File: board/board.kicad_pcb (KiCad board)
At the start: 2 copper layers, 66 x 48.3 mm, 93 parts, among them IC1 SN74LVC245APWR, IC2 SN74LVC245APWR, IC3 SN74LVC245APWR, IC4 SN74LVC245APWR, IC5 AP3417C, IC6 AP3417C, P1 CONN_02X16, P2 POWER, P3 JTAG, P4 HDMI-A, P5 CONN_01X03, SW1 SKRWAEE030, U1 10M08SCE144C8G, U2 ADV7513, U3 LFSPXO025560

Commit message: Schematics and Start of Board Layout
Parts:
- removed C10, C8: 4.7u, Capacitors_SMD:C_0805_HandSoldering
- removed C26, C27, C28, C29, C30, C35, C36, C37, C38, C39, C40, C41, C42, C43, C44, C45: 100nF, Capacitors_SMD:C_0805_HandSoldering
- removed C9: 10uF, Capacitors_SMD:C_0805_HandSoldering
- removed D1, D2: LED, LEDs:LED_0805
- removed F1: 0ZCK0050AF2E, Capacitors_SMD:C_0805_HandSoldering
- removed IC1, IC2, IC3, IC4: SN74LVC245APWR, Housings_SSOP:TSSOP-20_4.4x6.5mm_Pitch0.65mm
- removed IC5, IC6: AP3417C, TO_SOT_Packages_SMD:TSOT-23-5_HandSoldering
- removed L3, L4, L5, L6, L7: 10uH, Capacitors_SMD:C_0805_HandSoldering
- removed L8, L9: 2.2uH, Capacitors_SMD:C_0805_HandSoldering
- removed P1: CONN_02X16, Pin_Headers:Pin_Header_Straight_2x16_Pitch2.54mm
- removed P2: POWER, Pin_Headers:Pin_Header_Straight_1x02_Pitch2.54mm
- removed P3: JTAG, Pin_Headers:Pin_Header_Straight_2x05_Pitch2.54mm
- removed P4: HDMI-A, footprints:FCI_10029449-11-5B13-5DRLF
- removed P5: CONN_01X03, Pin_Headers:Pin_Header_Straight_1x03_Pitch2.54mm
- removed SW1: SKRWAEE030, Buttons_Switches_SMD:SW_SPST_EVPBF
- removed U1: 10M08SCE144C8G, footprints:QFP_144_GND
- removed U3: LFSPXO025560, Crystals:Crystal_SMD_EuroQuartz_MT-4pin_3.2x2.5mm_HandSoldering
- added AMP1: THS7316, Housings_SOIC:SOIC-8_3.9x4.9mm_Pitch1.27mm, B.Cu at (170.8, 95.2)
- added GPIO1: CONN_02X17, Pin_Headers:Pin_Header_Straight_2x17_Pitch2.54mm, F.Cu at (134.6, 104.1)
- added JTAG1: CONN_02X05, Pin_Headers:Pin_Header_Straight_2x05_Pitch2.54mm, F.Cu at (147.3, 66.0)
- added OSC1: XO32050UITA, Oscillators:Oscillator_SMD_EuroQuartz_XO32-4pin_3.2x2.5mm_HandSoldering, B.Cu at (140.3, 71.8)
- added POWER1: CONM_01x02, Pin_Headers:Pin_Header_Straight_1x02_Pitch2.54mm, F.Cu at (139.7, 96.5)
- added R22: 8k, Resistors_SMD:R_0805_HandSoldering, F.Cu at (149.2, 175.3)
- added R23: 16k, Resistors_SMD:R_0805_HandSoldering, F.Cu at (145.5, 110.0)
- added R24: 10k, Resistors_SMD:R_0805_HandSoldering, F.Cu at (135.3, 178.4)
- added R25: 10k, Resistors_SMD:R_0805_HandSoldering, F.Cu at (141.6, 179.7)
- added R26: 10k, Resistors_SMD:R_0805_HandSoldering, F.Cu at (149.9, 179.7)
- added R27: 75, Resistors_SMD:R_0805_HandSoldering, B.Cu at (175.3, 69.8)
- added R28: 75, Resistors_SMD:R_0805_HandSoldering, B.Cu at (176.3, 82.8)
- added R29: 75, Resistors_SMD:R_0805_HandSoldering, B.Cu at (176.5, 95.9)
- added RCA1: TrippleRCA, footprints:TrippleRCA, F.Cu at (181.6, 83.8)
- added REF**: MountingHole_3.2mm_M3_DIN965, Mounting_Holes:MountingHole_3.2mm_M3_DIN965, F.Cu at (141.0, 102.9)
- added REF**: MountingHole_3.2mm_M3_DIN965, Mounting_Holes:MountingHole_3.2mm_M3_DIN965, F.Cu at (141.0, 64.8)
- added REF**: MountingHole_3.2mm_M3_DIN965, Mounting_Holes:MountingHole_3.2mm_M3_DIN965, F.Cu at (163.8, 102.9)
- added REF**: MountingHole_3.2mm_M3_DIN965, Mounting_Holes:MountingHole_3.2mm_M3_DIN965, F.Cu at (163.8, 64.8)
- added REG1: LM1117IMPX-3.3, TO_SOT_Packages_SMD:SOT-223, B.Cu at (140.5, 85.6)
- C11, C12: value 10uF -> 100nF; moved to F.Cu
- C13, C14, C15, C16, C17, C18, C19, C2, C20, C21, C22, C23, C24, C25, C3, C31, C32, C33, C34, C4: moved to F.Cu
- C6: value 10uF -> 100nF
- C7: value 47u -> 100nF; footprint Capacitors_SMD:C_1206_HandSoldering -> Capacitors_SMD:C_0805_HandSoldering
- L1, L2: value 10uH -> 10mH
- R1: value 1K -> 1k
- R10, R11, R14: value 2K -> 10k; moved to B.Cu
- R12: value 10k -> 1k
- R13: value 2K -> 2k
- R15: value 2K -> 4k
- R16: value 1K -> 8k
- R17: value 450k 1% -> 16k
- R18: value 100k 1% -> 150
- R19: value 200k 1% -> 1k
- R2, R8: value 10k -> 150
- R20: value 100k 1% -> 2k
- R21, R4: value 10k -> 4k
- R3: value 10k -> 2k; moved to B.Cu
- R5: value 10k -> 8k; moved to B.Cu
- R6: value 10k -> 16k
- R7: value 10k -> 1k1; moved to B.Cu
- R9: value 887 1% -> 10k; moved to B.Cu
- U2: value ADV7513 -> 10M02SCE144; footprint Housings_QFP:LQFP-64-1EP_10x10mm_Pitch0.5mm -> footprints:QFP_144_GND
- moved C7 105.0 mm to (87.6, 91.4), turned to 0 degrees
- moved C2 100.8 mm to (87.6, 66.7), turned to 0 degrees
- moved C25 100.7 mm to (86.4, 179.1), turned to 0 degrees
- moved C3 99.7 mm to (87.6, 71.8), turned to 0 degrees
- moved C4 99.4 mm to (87.6, 76.2), turned to 0 degrees
- moved C12 98.8 mm to (87.0, 101.0), turned to 0 degrees
- moved C11 96.2 mm to (87.0, 95.9), turned to 0 degrees
- moved C24 93.4 mm to (87.0, 173.4), turned to 0 degrees
- moved C31 90.6 mm to (86.4, 183.5), turned to 0 degrees
- moved C23 87.1 mm to (86.4, 168.3), turned to 0 degrees
- moved L1 82.0 mm to (87.0, 105.4), turned to 0 degrees
- moved R21 81.4 mm to (142.2, 174.6)
- moved L2 80.6 mm to (86.4, 124.5), turned to 0 degrees
- moved C34 79.7 mm to (80.0, 117.5)
- moved C22 78.5 mm to (86.4, 163.8), turned to 0 degrees
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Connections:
- C1 pad 1: /3V3A -> Net-(C1-Pad1)
- C11 pad 1: /1V8B -> /3V3B
- C12 pad 1: /1V8C -> /3V3B
- C13 pad 1: /3V3A -> /3V3B
- C14 pad 1: /3V3A -> /3V3B
- C15 pad 1: /3V3A -> /3V3B
- C16 pad 1: /3V3A -> /3V3B
- C2 pad 1: /3V3B -> /3V3A
- C4 pad 1: /3V3D -> /3V3B
- C5 pad 1: /1V8A -> /3V3A
- C6 pad 1: GND -> /3V3A
- C6 pad 2: Net-(C6-Pad2) -> GND
- C7 pad 1: +5V -> GND
- C7 pad 2: GND -> /3V3A
- L1 pad 1: /3V3A -> /3V3B
- L1 pad 2: Net-(C6-Pad2) -> /3V3A
- L2 pad 1: /3V3B -> /3V3C
- L2 pad 2: Net-(C6-Pad2) -> /3V3A
- R1 pad 1: Net-(D1-Pad1) -> Net-(R1-Pad1)
- R1 pad 2: GND -> Net-(AMP1-Pad3)
- R10 pad 1: Net-(R10-Pad1) -> Net-(JTAG1-Pad9)
- R10 pad 2: /3V3D -> /3V3A
- R11 pad 2: /3V3D -> /3V3A
- R12 pad 1: GND -> Net-(R12-Pad1)
- R12 pad 2: Net-(P4-Pad19) -> Net-(AMP1-Pad2)
- R13 pad 1: Net-(P4-Pad16) -> Net-(R13-Pad1)
- R13 pad 2: +5V -> Net-(AMP1-Pad2)
- R14 pad 1: Net-(P4-Pad15) -> GND
- R14 pad 2: +5V -> Net-(JTAG1-Pad1)
- R15 pad 2: /3V3D -> Net-(AMP1-Pad2)
- R16 pad 1: Net-(D2-Pad1) -> Net-(R16-Pad1)
- R16 pad 2: GND -> Net-(AMP1-Pad2)
- R17 pad 1: Net-(C6-Pad2) -> Net-(R17-Pad1)
- R17 pad 2: Net-(IC5-Pad5) -> Net-(AMP1-Pad2)
- R18 pad 1: GND -> Net-(AMP1-Pad1)
- R18 pad 2: Net-(IC5-Pad5) -> GND
- R19 pad 1: Net-(C9-Pad2) -> Net-(R19-Pad1)
- R19 pad 2: Net-(IC6-Pad5) -> Net-(AMP1-Pad1)
- R2 pad 1: GND -> Net-(AMP1-Pad3)
- R2 pad 2: Net-(P3-Pad1) -> GND
- R20 pad 1: GND -> Net-(R20-Pad1)
- R20 pad 2: Net-(IC6-Pad5) -> Net-(AMP1-Pad1)
- R21 pad 1: /3V3D -> Net-(R21-Pad1)
- R21 pad 2: Net-(R21-Pad2) -> Net-(AMP1-Pad1)
- R3 pad 1: Net-(P3-Pad9) -> Net-(R3-Pad1)
- R3 pad 2: /3V3A -> Net-(AMP1-Pad3)
- R4 pad 1: Net-(P3-Pad5) -> Net-(R4-Pad1)
- R4 pad 2: /3V3A -> Net-(AMP1-Pad3)
- R5 pad 2: /3V3A -> Net-(AMP1-Pad3)
- R6 pad 2: /3V3B -> Net-(AMP1-Pad3)
- R7 pad 2: /3V3B -> Net-(AMP1-Pad2)
- R8 pad 1: Net-(R8-Pad1) -> Net-(AMP1-Pad2)
- R9 pad 1: GND -> Net-(JTAG1-Pad5)
- R9 pad 2: Net-(R9-Pad2) -> /3V3A
- U2 pad 1: /1V8A -> /3V3B
- U2 pad 10: GND -> Net-(U2-Pad10)
- U2 pad 11: /1V8A -> GND
- U2 pad 12: /1V8C -> /3V3B
- U2 pad 13: /1V8C -> Net-(R11-Pad1)
- U2 pad 14: Net-(R9-Pad2) -> Net-(U2-Pad14)
- U2 pad 15: /1V8B -> Net-(JTAG1-Pad5)
- U2 pad 16: Net-(P4-Pad19) -> Net-(JTAG1-Pad1)
- U2 pad 17: Net-(P4-Pad12) -> Net-(JTAG1-Pad9)
- U2 pad 19: /1V8B -> Net-(U2-Pad19)
- U2 pad 2: Net-(U1-Pad75) -> /3V3C
- U2 pad 20: Net-(P4-Pad9) -> GND
- U2 pad 22: GND -> /3V3B
- U2 pad 25: /1V8B -> Net-(OSC1-Pad3)
- U2 pad 28: Net-(R15-Pad1) -> Net-(GPIO1-Pad33)
- U2 pad 29: /3V3D -> /3V3B
- U2 pad 31: /1V8A -> Net-(U2-Pad31)
- U2 pad 32: GND -> Net-(GPIO1-Pad32)
- U2 pad 33: Net-(P4-Pad15) -> Net-(GPIO1-Pad31)
- U2 pad 34: Net-(P4-Pad16) -> /3V3C
- U2 pad 35: Net-(R10-Pad1) -> /3V3C
- U2 pad 36: Net-(R11-Pad1) -> /3V3B
- U2 pad 37: Net-(U1-Pad111) -> /3V3B
- U2 pad 38: Net-(U1-Pad110) -> GND
- U2 pad 4: GND -> Net-(U2-Pad4)
- U2 pad 43: Net-(U1-Pad100) -> /3V3B
- U2 pad 45: Net-(U1-Pad98) -> GND
- U2 pad 5: GND -> Net-(U2-Pad5)
- U2 pad 51: /1V8A -> Net-(GPIO1-Pad20)
- U2 pad 56: Net-(U1-Pad86) -> /3V3B
- U2 pad 57: Net-(U1-Pad85) -> GND
- U2 pad 58: Net-(U1-Pad84) -> /3V3B
- U2 pad 6: GND -> Net-(U2-Pad6)
- U2 pad 64: Net-(U1-Pad76) -> /3V3B
- U2 pad 65: GND -> Net-(GPIO1-Pad10)
- U2 pad 7: GND -> Net-(U2-Pad7)
- U2 pad 8: GND -> Net-(U2-Pad8)
- U2 pad 9: GND -> Net-(U2-Pad9)
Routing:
- net /3V3B: track 211.6 -> 0.00 mm, vias 18 -> 0
- net GND: track 132.0 -> 0.00 mm, vias 42 -> 1
- net /3V3C: track 108.8 -> 0.00 mm, vias 12 -> 0
- net +5V: track 69.7 -> 0.00 mm, vias 3 -> 0
- net /3V3D: track 64.0 -> 0.00 mm, vias 6 -> 0
- net /1V8A: track 61.9 -> 0.00 mm, vias 5 -> 0
- net Net-(R15-Pad1): track 41.8 -> 0.00 mm, vias 4 -> 0
- net Net-(R21-Pad2): track 38.3 -> 0.00 mm, vias 2 -> 0
- net /1V8B: track 34.6 -> 0.00 mm, vias 6 -> 0
- net Net-(P4-Pad16): track 32.1 -> 0.00 mm, vias 2 -> 0
- net Net-(AMP1-Pad8): track 0.00 -> 31.7 mm, vias 0 -> 2
- net Net-(R10-Pad1): track 30.4 -> 0.00 mm, vias 2 -> 0
- net Net-(P4-Pad15): track 28.5 -> 0.00 mm, vias 2 -> 0
- net Net-(P3-Pad5): track 27.6 -> 0.00 mm
- net /1V8C: track 25.9 -> 0.00 mm, vias 4 -> 0
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- removed copper zone on B.Cu, net GND
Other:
- board size 66 x 48.3 mm -> 49.5 x 45.7 mm
- board text removed: "D-Video Board Rev. 1 2017-03-04"
- board text removed: "U1"

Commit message: Board layout finished
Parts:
- removed the REF** at (141.0, 102.9)
- removed the REF** at (141.0, 64.8)
- removed the REF** at (163.8, 102.9)
- removed the REF** at (163.8, 64.8)
- added C26: 100nF, Capacitors_SMD:C_0603_HandSoldering, F.Cu at (141.7, 109.7)
- added C27: 100nF, Capacitors_SMD:C_0603_HandSoldering, F.Cu at (139.7, 104.1)
- added C28: 100nF, Capacitors_SMD:C_0603_HandSoldering, F.Cu at (139.7, 99.8)
- added C29: 100nF, Capacitors_SMD:C_0603_HandSoldering, F.Cu at (139.7, 94.5)
- added C30: 100nF, Capacitors_SMD:C_0603_HandSoldering, F.Cu at (139.7, 102.9)
- added C8: 10uF, Capacitors_SMD:C_0805_HandSoldering, F.Cu at (121.9, 120.7)
- added GPIO2: CONN_02X05, Pin_Headers:Pin_Header_Straight_2x05_Pitch2.54mm, F.Cu at (132.1, 76.2)
- added REF**: MountingHole_3.2mm_M3, Mounting_Holes:MountingHole_3.2mm_M3, F.Cu at (154.9, 73.7)
- added REF**: MountingHole_3.2mm_M3, Mounting_Holes:MountingHole_3.2mm_M3, F.Cu at (154.9, 121.9)
- C1, C5, REG1: moved to F.Cu
- C11, C12, C13, C14, C15, C16, C17, C18, C19, C20, C21, C22, C23, C24, C25, C31, C32, C33, C34: footprint Capacitors_SMD:C_0805_HandSoldering -> Capacitors_SMD:C_0603_HandSoldering
- C6: footprint Capacitors_SMD:C_0805_HandSoldering -> Capacitors_SMD:C_0603_HandSoldering; moved to F.Cu
- C7: footprint Capacitors_SMD:C_0805_HandSoldering -> Capacitors_SMD:C_0603_HandSoldering; moved to B.Cu
- GPIO1: value CONN_02X17 -> CONN_02X08; footprint Pin_Headers:Pin_Header_Straight_2x17_Pitch2.54mm -> Pin_Headers:Pin_Header_Straight_2x08_Pitch2.54mm
- R1, R12, R13, R15, R16, R17, R18, R19, R2, R20, R21, R22, R23, R24, R25, R26, R4, R6, R8, U2: moved to B.Cu
- moved C31 107.3 mm to (137.4, 89.2), turned to 180 degrees
- moved R24 87.4 mm to (118.1, 92.7), turned to 270 degrees
- moved C25 86.8 mm to (136.9, 108.5), turned to 90 degrees
- moved R25 84.0 mm to (118.1, 99.1), turned to 90 degrees
- moved R26 80.8 mm to (118.1, 105.4), turned to 90 degrees
- moved C24 78.3 mm to (130.8, 108.5), turned to 90 degrees
- moved C23 72.0 mm to (126.5, 108.5), turned to 90 degrees
- moved C7 69.7 mm to (156.2, 78.7), turned to 180 degrees
- moved R12 67.6 mm to (149.2, 98.4)
- moved R16 67.1 mm to (154.3, 104.8)
- moved L2 66.3 mm to (139.7, 85.1), turned to 90 degrees
- moved R13 66.3 mm to (154.3, 98.4)
- moved R21 65.9 mm to (154.3, 109.9)
- moved C22 65.3 mm to (120.9, 108.5), turned to 270 degrees
- moved C21 65.2 mm to (124.0, 106.2)
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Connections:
- C5 pad 1: /3V3A -> GND
- C5 pad 2: GND -> /3V3A
- REG1 pad 2: /3V3A -> Net-(REG1-Pad2)
- U2 pad 100: Net-(R19-Pad1) -> Net-(U2-Pad100)
- U2 pad 101: Net-(R20-Pad1) -> Net-(U2-Pad101)
- U2 pad 103: Net-(R21-Pad1) -> Net-(U2-Pad103)
- U2 pad 105: Net-(R22-Pad1) -> Net-(U2-Pad105)
- U2 pad 106: Net-(R23-Pad1) -> Net-(U2-Pad106)
- U2 pad 25: Net-(OSC1-Pad3) -> Net-(GPIO2-Pad4)
- U2 pad 27: Net-(GPIO1-Pad34) -> Net-(GPIO2-Pad6)
- U2 pad 28: Net-(GPIO1-Pad33) -> Net-(GPIO2-Pad7)
- U2 pad 32: Net-(GPIO1-Pad32) -> Net-(GPIO2-Pad9)
- U2 pad 33: Net-(GPIO1-Pad31) -> Net-(GPIO2-Pad10)
- U2 pad 39: Net-(GPIO1-Pad30) -> Net-(R1-Pad1)
- U2 pad 40: Net-(GPIO1-Pad29) -> Net-(R3-Pad1)
- U2 pad 41: Net-(GPIO1-Pad28) -> Net-(R4-Pad1)
- U2 pad 42: Net-(GPIO1-Pad27) -> Net-(R5-Pad1)
- U2 pad 44: Net-(GPIO1-Pad26) -> Net-(R6-Pad1)
- U2 pad 46: Net-(GPIO1-Pad25) -> Net-(R7-Pad1)
- U2 pad 47: Net-(GPIO1-Pad24) -> Net-(R12-Pad1)
- U2 pad 48: Net-(GPIO1-Pad23) -> Net-(R13-Pad1)
- U2 pad 49: Net-(GPIO1-Pad22) -> Net-(U2-Pad49)
- U2 pad 50: Net-(GPIO1-Pad21) -> Net-(U2-Pad50)
- U2 pad 51: Net-(GPIO1-Pad20) -> Net-(U2-Pad51)
- U2 pad 52: Net-(GPIO1-Pad19) -> Net-(U2-Pad52)
- U2 pad 53: Net-(GPIO1-Pad18) -> Net-(U2-Pad53)
- U2 pad 54: Net-(GPIO1-Pad17) -> Net-(U2-Pad54)
- U2 pad 55: Net-(GPIO1-Pad16) -> Net-(U2-Pad55)
- U2 pad 59: Net-(GPIO1-Pad15) -> Net-(U2-Pad59)
- U2 pad 60: Net-(GPIO1-Pad14) -> Net-(U2-Pad60)
- U2 pad 61: Net-(GPIO1-Pad13) -> Net-(R15-Pad1)
- U2 pad 62: Net-(GPIO1-Pad12) -> Net-(R16-Pad1)
- U2 pad 63: Net-(GPIO1-Pad11) -> Net-(R17-Pad1)
- U2 pad 65: Net-(GPIO1-Pad10) -> Net-(R19-Pad1)
- U2 pad 67: Net-(GPIO1-Pad9) -> Net-(R20-Pad1)
- U2 pad 68: Net-(GPIO1-Pad8) -> Net-(R21-Pad1)
- U2 pad 69: Net-(GPIO1-Pad7) -> Net-(R22-Pad1)
- U2 pad 70: Net-(GPIO1-Pad6) -> Net-(R23-Pad1)
- U2 pad 74: Net-(GPIO1-Pad5) -> Net-(GPIO1-Pad16)
- U2 pad 75: Net-(GPIO1-Pad4) -> Net-(GPIO1-Pad15)
- U2 pad 76: Net-(GPIO1-Pad3) -> Net-(GPIO1-Pad14)
- U2 pad 77: Net-(U2-Pad77) -> Net-(GPIO1-Pad13)
- U2 pad 78: Net-(R1-Pad1) -> Net-(GPIO1-Pad12)
- U2 pad 79: Net-(R3-Pad1) -> Net-(GPIO1-Pad11)
- U2 pad 80: Net-(U2-Pad80) -> Net-(GPIO1-Pad10)
- U2 pad 81: Net-(R4-Pad1) -> Net-(GPIO1-Pad9)
- U2 pad 84: Net-(U2-Pad84) -> Net-(GPIO1-Pad8)
- U2 pad 85: Net-(R5-Pad1) -> Net-(GPIO1-Pad7)
- U2 pad 86: Net-(U2-Pad86) -> Net-(GPIO1-Pad6)
- U2 pad 87: Net-(R6-Pad1) -> Net-(GPIO1-Pad5)
- U2 pad 88: Net-(U2-Pad88) -> Net-(GPIO1-Pad4)
- U2 pad 89: Net-(R7-Pad1) -> Net-(GPIO1-Pad3)
- U2 pad 91: Net-(R12-Pad1) -> Net-(OSC1-Pad3)
- U2 pad 92: Net-(R13-Pad1) -> Net-(U2-Pad92)
- U2 pad 95: Net-(R15-Pad1) -> Net-(U2-Pad95)
- U2 pad 97: Net-(R16-Pad1) -> Net-(U2-Pad97)
- U2 pad 98: Net-(R17-Pad1) -> Net-(U2-Pad98)
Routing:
- net /3V3B: track 0.00 -> 190.5 mm, vias 0 -> 21
- net /3V3C: track 0.00 -> 87.0 mm, vias 0 -> 9
- net Net-(AMP1-Pad2): track 0.00 -> 47.7 mm, vias 0 -> 2
- net Net-(AMP1-Pad1): track 0.00 -> 47.3 mm, vias 0 -> 2
- net GND: track 0.00 -> 39.5 mm, vias 1 -> 21
- net Net-(R29-Pad1): track 4.41 -> 38.7 mm, vias 0 -> 1
- net Net-(AMP1-Pad3): track 0.00 -> 32.5 mm
- net Net-(AMP1-Pad8): track 31.7 -> 4.36 mm, vias 2 -> 0
- net Net-(GPIO1-Pad34): track 26.1 -> 0.00 mm
- net Net-(R28-Pad1): track 3.45 -> 27.2 mm, vias 0 -> 1
- net Net-(GPIO1-Pad32): track 21.8 -> 0.00 mm
- net Net-(GPIO1-Pad33): track 21.1 -> 0.00 mm
- net Net-(GPIO2-Pad10): track 0.00 -> 18.2 mm
- net Net-(GPIO2-Pad8): track 0.00 -> 17.6 mm
- net Net-(GPIO2-Pad6): track 0.00 -> 17.3 mm
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- added copper zone on F.Cu, net GND
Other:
- board size 49.5 x 45.7 mm -> 43.2 x 53.3 mm
- rule trace_min: 0.2 -> 0.25
- board text added: "A-Video Board Rev. 1"

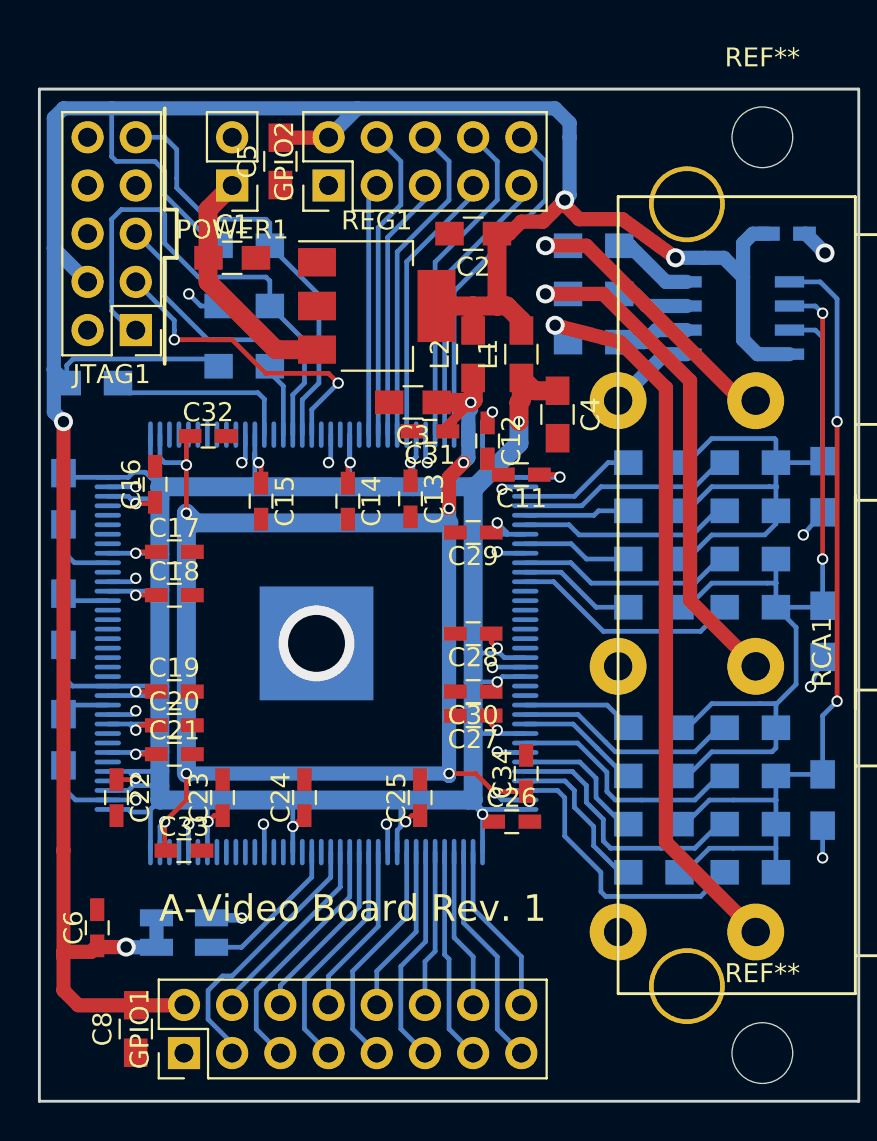
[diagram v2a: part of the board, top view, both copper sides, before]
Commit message: Adapter board for ZX Spectrum
Plus some changes to the A-Video board itself to better fit the needs of
the ZX Spectrum mod (which currently drives the development)
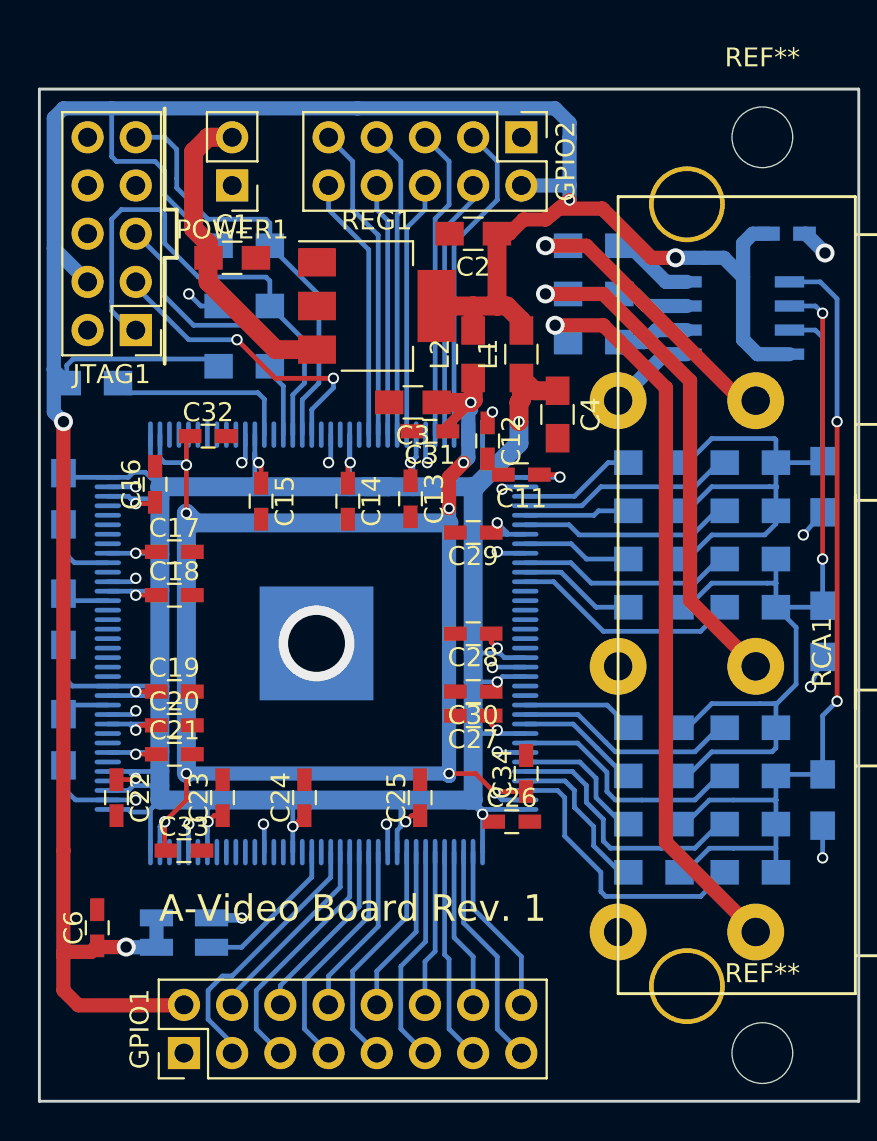
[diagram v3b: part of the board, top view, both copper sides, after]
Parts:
- removed C5, C8: 10uF, Capacitors_SMD:C_0805_HandSoldering
- moved GPIO2 10.5 mm to (142.2, 73.7), turned to 270 degrees
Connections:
- POWER1 pad 1: Net-(C1-Pad1) -> GND
- POWER1 pad 2: GND -> Net-(C1-Pad1)
- U2 pad 24: Net-(GPIO2-Pad3) -> Net-(GPIO2-Pad10)
- U2 pad 25: Net-(GPIO2-Pad4) -> Net-(GPIO2-Pad9)
- U2 pad 26: Net-(GPIO2-Pad5) -> Net-(GPIO2-Pad8)
- U2 pad 27: Net-(GPIO2-Pad6) -> Net-(GPIO2-Pad7)
- U2 pad 28: Net-(GPIO2-Pad7) -> Net-(GPIO2-Pad6)
- U2 pad 31: Net-(GPIO2-Pad8) -> Net-(GPIO2-Pad5)
- U2 pad 32: Net-(GPIO2-Pad9) -> Net-(GPIO2-Pad4)
- U2 pad 33: Net-(GPIO2-Pad10) -> Net-(GPIO2-Pad3)
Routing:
- net Net-(GPIO2-Pad8): track 17.6 -> 13.4 mm
- net Net-(GPIO2-Pad10): track 18.2 -> 14.0 mm
- net Net-(C1-Pad1): track 12.8 -> 16.8 mm
- net Net-(GPIO2-Pad3): track 13.3 -> 17.1 mm
- net Net-(GPIO2-Pad6): track 17.3 -> 14.3 mm
- net Net-(GPIO2-Pad5): track 13.9 -> 16.5 mm
- net Net-(GPIO2-Pad4): track 16.7 -> 14.3 mm
- net Net-(GPIO2-Pad9): track 14.8 -> 16.8 mm
- net Net-(JTAG1-Pad5): track 15.3 -> 17.0 mm
- net Net-(GPIO2-Pad7): track 14.6 -> 16.3 mm
- net /3V3A: track 154.8 -> 153.7 mm
- net Net-(JTAG1-Pad3): track 16.8 -> 16.1 mm

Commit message: small additions for zx spectrum mod
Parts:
- added POWER2: CONN_02X01, Pin_Headers:Pin_Header_Straight_1x02_Pitch2.54mm, F.Cu at (129.5, 76.2)
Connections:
- JTAG1 pad 6: Net-(JTAG1-Pad6) -> (no net)
- JTAG1 pad 7: Net-(JTAG1-Pad7) -> (no net)
- JTAG1 pad 8: Net-(JTAG1-Pad8) -> (no net)
- REG1 pad 2: Net-(REG1-Pad2) -> (no net)
- U2 pad 10: Net-(U2-Pad10) -> (no net)
- U2 pad 100: Net-(U2-Pad100) -> (no net)
- U2 pad 101: Net-(U2-Pad101) -> (no net)
- U2 pad 103: Net-(U2-Pad103) -> (no net)
- U2 pad 105: Net-(U2-Pad105) -> (no net)
- U2 pad 106: Net-(U2-Pad106) -> (no net)
- U2 pad 112: Net-(U2-Pad112) -> (no net)
- U2 pad 114: Net-(U2-Pad114) -> (no net)
- U2 pad 116: Net-(U2-Pad116) -> (no net)
- U2 pad 117: Net-(U2-Pad117) -> (no net)
- U2 pad 123: Net-(U2-Pad123) -> (no net)
- U2 pad 124: Net-(U2-Pad124) -> (no net)
- U2 pad 125: Net-(U2-Pad125) -> (no net)
- U2 pad 126: Net-(U2-Pad126) -> (no net)
- U2 pad 127: Net-(U2-Pad127) -> (no net)
- U2 pad 128: Net-(U2-Pad128) -> (no net)
- U2 pad 129: Net-(U2-Pad129) -> (no net)
- U2 pad 130: Net-(U2-Pad130) -> (no net)
- U2 pad 134: Net-(U2-Pad134) -> (no net)
- U2 pad 137: Net-(U2-Pad137) -> (no net)
- U2 pad 138: Net-(U2-Pad138) -> (no net)
- U2 pad 139: Net-(U2-Pad139) -> (no net)
- U2 pad 14: Net-(U2-Pad14) -> (no net)
- U2 pad 140: Net-(U2-Pad140) -> (no net)
- U2 pad 141: Net-(U2-Pad141) -> (no net)
- U2 pad 19: Net-(U2-Pad19) -> (no net)
- U2 pad 21: Net-(U2-Pad21) -> (no net)
- U2 pad 23: Net-(U2-Pad23) -> (no net)
- U2 pad 3: Net-(U2-Pad3) -> (no net)
- U2 pad 4: Net-(U2-Pad4) -> (no net)
- U2 pad 49: Net-(U2-Pad49) -> (no net)
- U2 pad 5: Net-(U2-Pad5) -> (no net)
- U2 pad 50: Net-(U2-Pad50) -> (no net)
- U2 pad 51: Net-(U2-Pad51) -> (no net)
- U2 pad 52: Net-(U2-Pad52) -> (no net)
- U2 pad 53: Net-(U2-Pad53) -> (no net)
- U2 pad 54: Net-(U2-Pad54) -> (no net)
- U2 pad 55: Net-(U2-Pad55) -> (no net)
- U2 pad 59: Net-(U2-Pad59) -> (no net)
- U2 pad 6: Net-(U2-Pad6) -> (no net)
- U2 pad 60: Net-(U2-Pad60) -> (no net)
- U2 pad 7: Net-(U2-Pad7) -> (no net)
- U2 pad 8: Net-(U2-Pad8) -> (no net)
- U2 pad 9: Net-(U2-Pad9) -> (no net)
- U2 pad 90: Net-(U2-Pad90) -> (no net)
- U2 pad 92: Net-(U2-Pad92) -> (no net)
- U2 pad 94: Net-(U2-Pad94) -> (no net)
- U2 pad 95: Net-(U2-Pad95) -> (no net)
- U2 pad 97: Net-(U2-Pad97) -> (no net)
- U2 pad 98: Net-(U2-Pad98) -> (no net)
- U2 pad 99: Net-(U2-Pad99) -> (no net)
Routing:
- net Net-(C1-Pad1): track 16.8 -> 19.3 mm

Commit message: gerber files for PCB manufacture
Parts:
- GND VIN: renamed from POWER1
- renumbered REF** to ?, POWER2 to ?
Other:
- board text added: "A-Video Board Rev. 1 2017-11-01"
- board text removed: "A-Video Board Rev. 1"
